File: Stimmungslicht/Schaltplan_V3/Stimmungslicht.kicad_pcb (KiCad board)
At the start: 2 copper layers, 37.8 x 37.8 mm, 19 parts, among them IC1 STM32G031J6M6, J1 Conn_01x01, J2 Conn_01x04_Male, U1 HU2032-LF, U101 Touch_Sens_Pad, U102 Touch_Sens_Pad, U103 Touch_Sens_Pad, U104 Touch_Sens_Pad

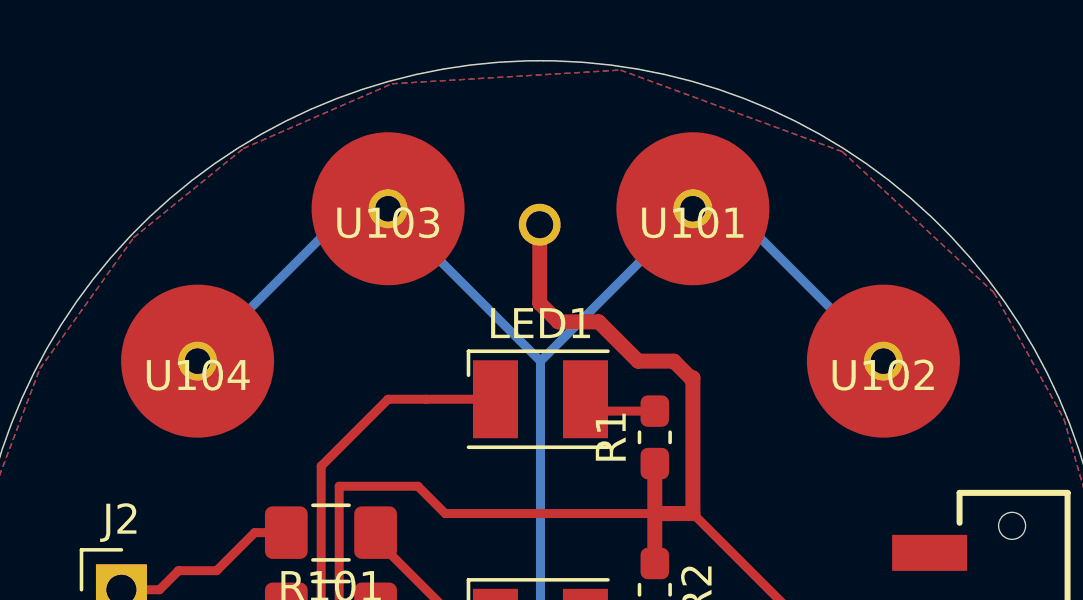
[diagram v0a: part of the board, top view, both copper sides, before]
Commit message: Konataktierungen ergäntzt
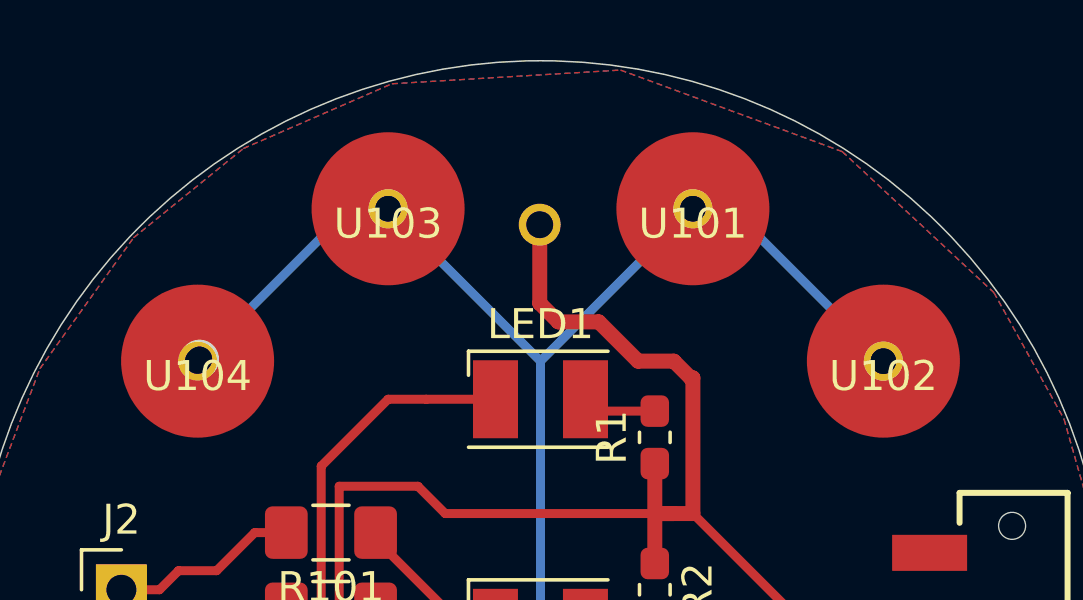
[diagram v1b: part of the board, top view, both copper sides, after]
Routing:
- net Net-(JP101-Pad1): vias 0 -> 4
